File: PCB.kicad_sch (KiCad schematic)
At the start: 34 parts, among them J1 USB_C_Receptacle_USB2.0, J2 JST - 1.00mm 4 Pin, SW72 SW_Push, SW73 SW_Push, U1 RP2040, U2 MX25R3235FZNxx0, U3 USBLC6-2SC6, U4 AP2127N3-1.2, Y1 Crystal_GND24_Small

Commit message: Updated LCSC part numbers for all parts.
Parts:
- C1, C2: value 15p -> 30p; footprint Capacitor_SMD:C_0201_0603Metric -> Capacitor_SMD:C_0402_1005Metric; LCSC (none) -> C1562
- C10, C12, C13, C15, C3: footprint Capacitor_SMD:C_0201_0603Metric -> Capacitor_SMD:C_0402_1005Metric; LCSC (none) -> C52923
- C11, C14, C16, C4, C5, C6, C7, C8, C9: footprint Capacitor_SMD:C_0201_0603Metric -> Capacitor_SMD:C_0402_1005Metric; LCSC (none) -> C1525
- F1: value 1A -> 700mA; footprint (none) -> Fuse:Fuse_0402_1005Metric; LCSC (none) -> C914086
- FB1: footprint (none) -> Inductor_SMD:L_0402_1005Metric; LCSC (none) -> C85812
- J1: footprint (none) -> Connector_USB:USB_C_Receptacle_GCT_USB4085
- J2: LCSC (none) -> C160404
- R1, R2: footprint Resistor_SMD:R_0201_0603Metric -> Resistor_SMD:R_0402_1005Metric; LCSC (none) -> C25152
- R3: footprint Resistor_SMD:R_0201_0603Metric -> Resistor_SMD:R_0402_1005Metric; LCSC (none) -> C106235
- R4, R5: footprint (none) -> Resistor_SMD:R_0402_1005Metric; LCSC (none) -> C25905
- R7: LCSC C25082 -> (none)
- SW72, SW73: LCSC (none) -> C115351
- U1: LCSC (none) -> C2040
- U2: value MX25R3235FZNxx0 -> SOP-8 SPI FLASH
- U3: LCSC (none) -> C558442
- U4: value AP2127N3-1.2 -> 3.3V Fixed Regulator; LCSC (none) -> C150715
- Y1: value Crystal_GND24_Small -> 12MHz Crystal 3225; LCSC (none) -> C9002

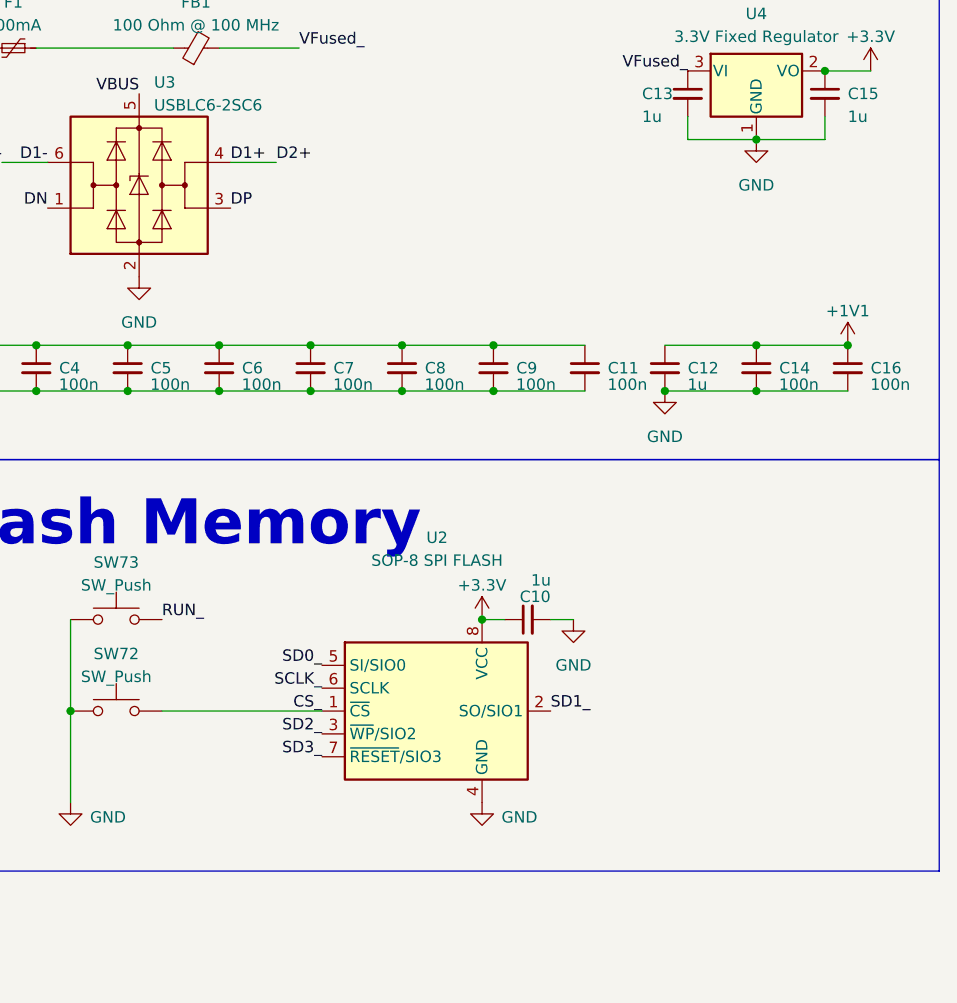
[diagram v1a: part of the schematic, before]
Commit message: Added missing decoupling capacitor and cr created example layout.
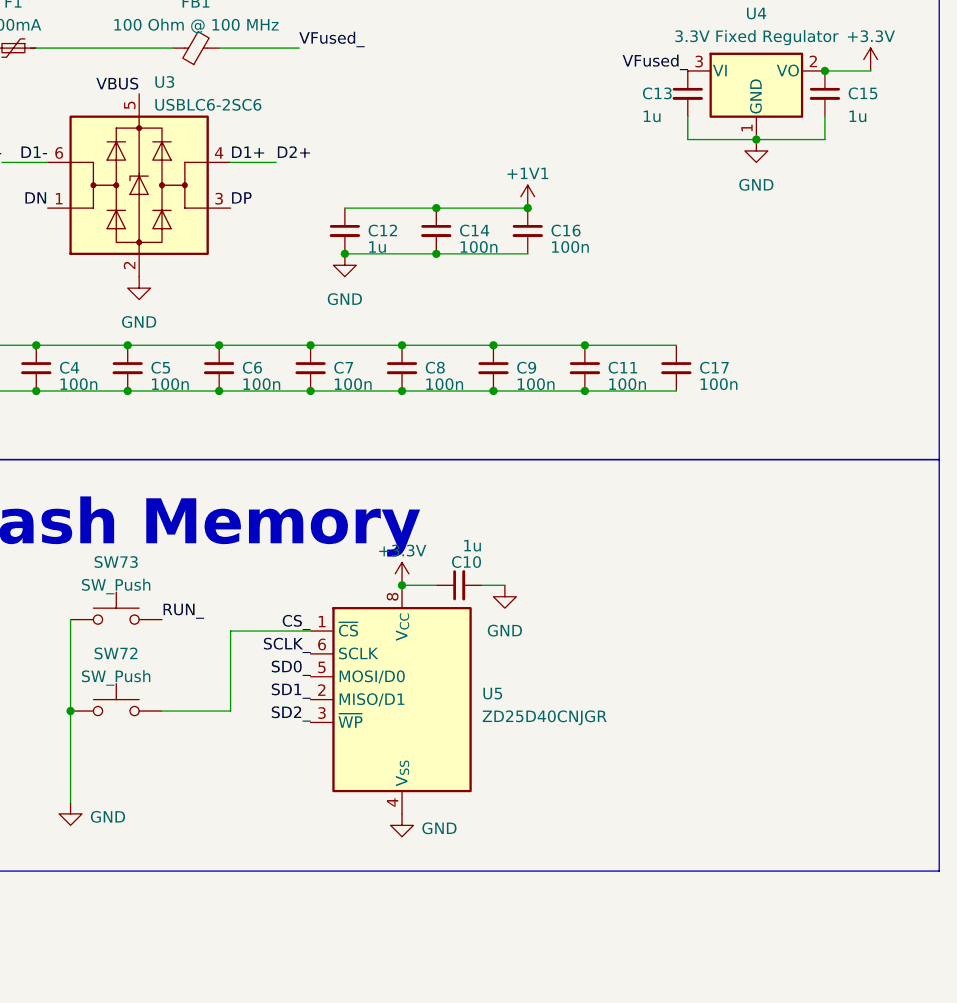
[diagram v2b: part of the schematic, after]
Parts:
- removed U2: SOP-8 SPI FLASH, Package_SO:SOP-8_3.76x4.96mm_P1.27mm, symbol Memory_Flash:MX25R3235FZNxx0
- added C17: 100n, Capacitor_SMD:C_0402_1005Metric, symbol Device:C_Small
- added U5: ZD25D40CNJGR, USON8:USON-8_1.5x1.5mm_P0.45mm, symbol Flash_NOR_SPI:ZD25D40CNJGR
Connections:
- net +3.3V: now also C17.1, U5.8 (V_{CC})
- net CS_: now also U5.1 (~{CS})
- net GND: now also C17.2, U5.4 (V_{SS}), U5.9 (PAD/V_{SS})
- net SCLK_: now also U5.6 (SCLK)
- net SD0_: now also U5.5 (MOSI/D0)
- net SD1_: now also U5.2 (MISO/D1)
- net SD2_: now also U5.3 (~{WP})
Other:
- moved on the sheet: C12, C14, C16
